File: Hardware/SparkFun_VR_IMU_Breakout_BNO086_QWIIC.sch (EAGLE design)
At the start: 41 parts, among them J2 SMD, J3 PTH, J4 SMD, J6 SPI, U2 BNO080, Y1 32.768kHz

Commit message: some more final changes
-added name to revisioner on sch and brd
-moved sch section names to symbol layer, added IMU name
-fixed two DRC errors (angle and stub)
-added more GND vias
-Axis labels - break linear line to show rotation line going over
-Larger SFE flame logo
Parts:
- LOGO4: value SFE_LOGO_FLAME.1_INCH -> SFE_LOGO_FLAME.2_INCH; device SparkFun-Aesthetics:SFE_LOGO_FLAME.1_INCH -> SparkFun-Aesthetics:SFE_LOGO_FLAME.2_INCH
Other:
- note added: "A. England, P. Lewis"
- note added: "IMU"
- note removed: "A. England"

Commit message: 3V3 net to thicker trace and more
-upped 3v3 trace to 20mil
-nudges some vias/traces for better GND flow
-added more gnd vias
-reduced GND pour isolates from 12 to 10
-I2C pullup jumper changes to NC trace
-updated IC to 086, in temp library for now
-added Power LED jumper
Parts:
- added LED: JUMPER-SMT_2_NC_TRACE_SILK, SparkFun-Jumpers:JUMPER-SMT_2_NC_TRACE_SILK
- I2C: value JUMPER-SMT_3_2-NC_PASTE_SILK -> JUMPER-SMT_3_2-NC_TRACE_SILK; device SparkFun-Jumpers:JUMPER-SMT_3_2-NC_PASTE_SILK -> SparkFun-Jumpers:JUMPER-SMT_3_2-NC_TRACE_SILK
- U2: value BNO080 -> BNO086; device SparkFun-IC-Special-Function:BNO080 -> bno086:BNO086
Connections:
- new net N$4: LED.2, PWR.A
- net 3.3V: now also LED.1; no longer PWR.A
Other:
- note added: "Clear I2C Jumper when using SPI or UART"
- note added: "Clear LED Jumper to disable Power LED"
- note added: "Power LED"
- note removed: "Clear SJ1 when using SPI or UART"
- moved on the sheet: J1, J6, PS0, PS1, PWR, R2, R7, R8

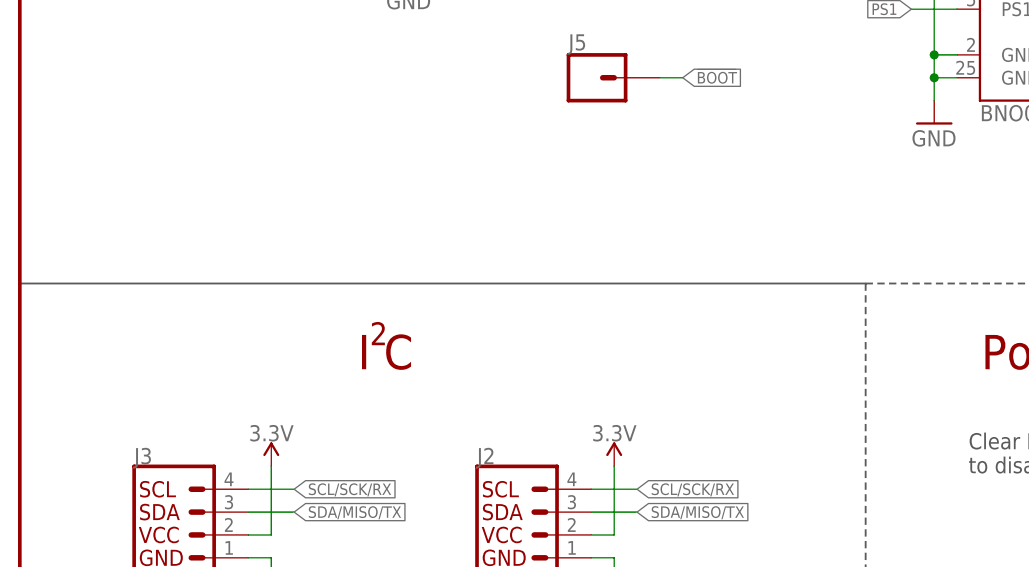
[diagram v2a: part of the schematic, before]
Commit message: line in sch to dash, address options in silk
-corrected a line in SCH to match others as dashed
-Added bottom silk to show address options
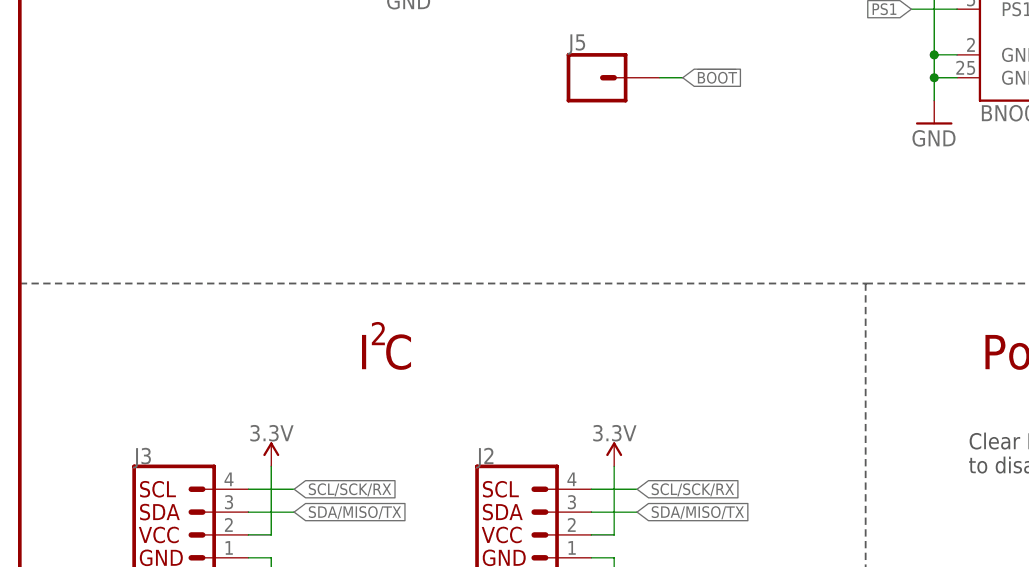
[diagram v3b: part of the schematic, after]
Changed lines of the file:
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@@
 <text x="170.18" y="83.82" size="3.81" layer="94" font="vector" align="center">SPI</text>
 <text x="39.878" y="85.852" size="2.54" layer="94" font="vector" align="center">2</text>
-<wire x1="0" y1="91.44" x2="93.98" y2="91.44" width="0.2032" layer="97"/>
+<wire x1="0" y1="91.44" x2="93.98" y2="91.44" width="0.2032" layer="97" style="longdash"/>
 <wire x1="93.98" y1="91.44" x2="147.32" y2="91.44" width="0.2032" layer="97" style="longdash"/>
 <wire x1="147.32" y1="91.44" x2="193.04" y2="91.44" width="0.2032" layer="97" style="longdash"/>
